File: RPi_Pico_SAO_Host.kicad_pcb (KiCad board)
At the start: 2 copper layers, 42 x 51.5 mm, 11 parts, among them J1 SAO Host Header, J2 SAO Host Header

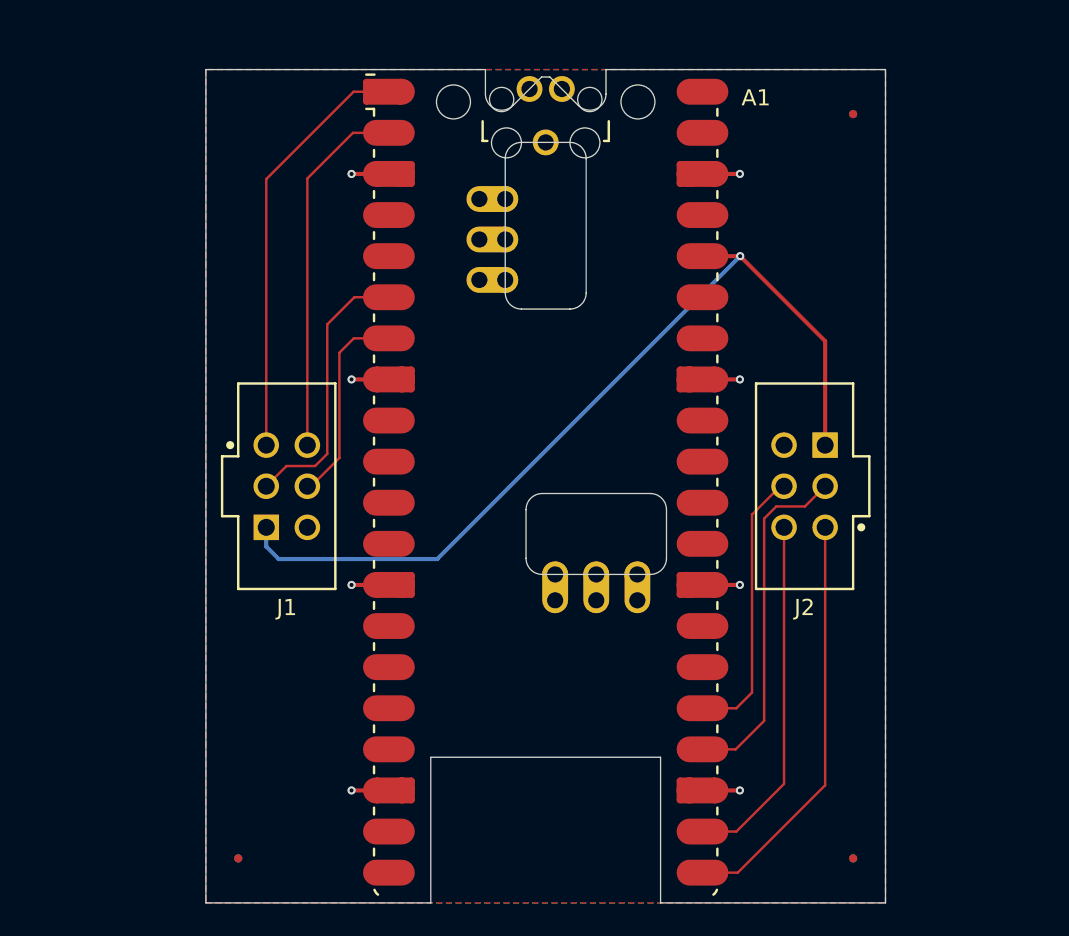
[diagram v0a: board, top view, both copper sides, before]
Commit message: Add v2 design changes
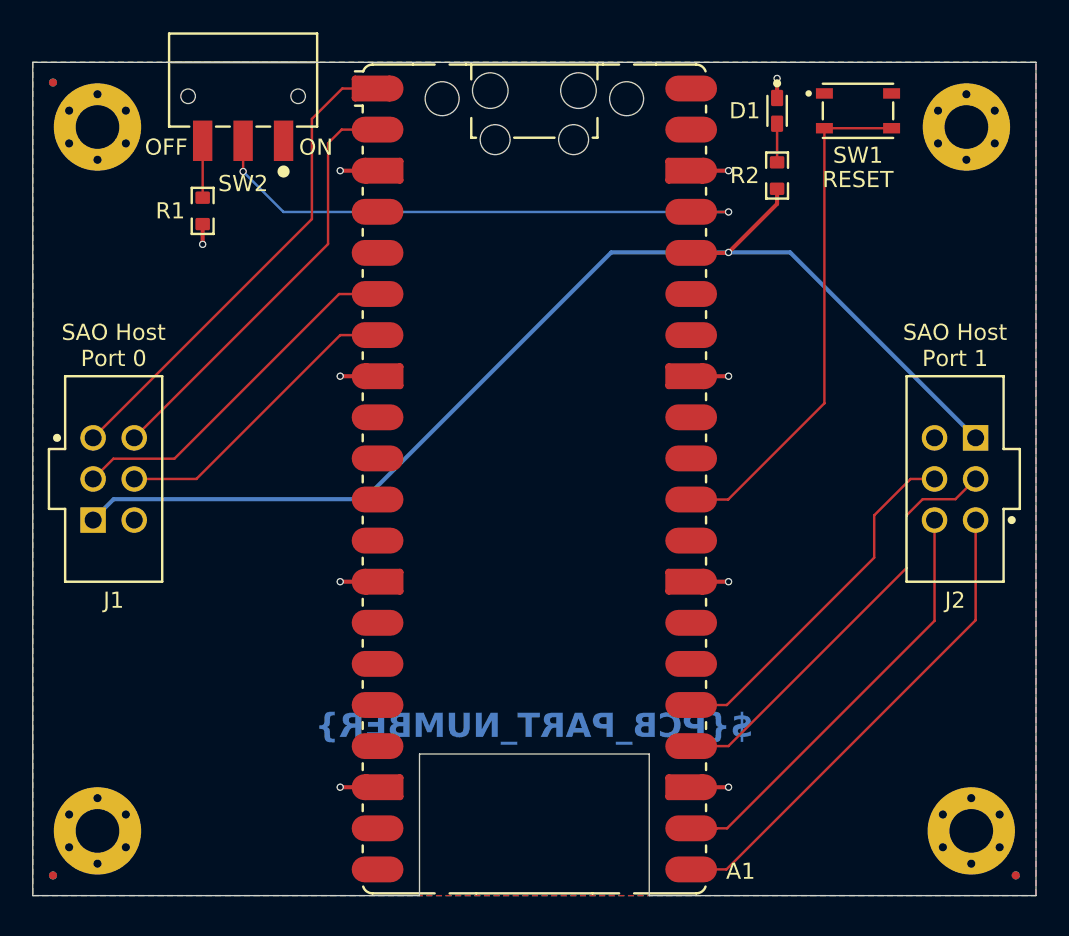
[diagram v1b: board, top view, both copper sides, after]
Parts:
- added D1: Green, CGND_LED:LEDSC_0603_0.8x1.6x0.8mm_L0.45x0.7mm_N, F.Cu at (154.0, 85.0)
- added H1: MTGNP_H2.1mm_M3.8mm_K4.2mm, CGND_Mounting_Hole:MTGNP_H2.1mm_M3.8mm_K4.2mm, F.Cu at (133.3, 84.2)
- added H2: MTGNP_H2.1mm_M3.8mm_K4.2mm, CGND_Mounting_Hole:MTGNP_H2.1mm_M3.8mm_K4.2mm, F.Cu at (144.7, 84.2)
- added H3: MTGP_5.4mm_H2.7mm_6V_H0.5mm, CGND_Mounting_Hole:MTGP_5.4mm_H2.7mm_6V_H0.5mm, F.Cu at (165.7, 86.0)
- added H4: MTGP_5.4mm_H2.7mm_6V_H0.5mm, CGND_Mounting_Hole:MTGP_5.4mm_H2.7mm_6V_H0.5mm, F.Cu at (166.0, 129.5)
- added H5: MTGP_5.4mm_H2.7mm_6V_H0.5mm, CGND_Mounting_Hole:MTGP_5.4mm_H2.7mm_6V_H0.5mm, F.Cu at (112.0, 129.5)
- added H6: MTGP_5.4mm_H2.7mm_6V_H0.5mm, CGND_Mounting_Hole:MTGP_5.4mm_H2.7mm_6V_H0.5mm, F.Cu at (112.0, 86.0)
- added LOGO3: Logo_WEEE_5.63x8mm_Silkscreen, CGND_Graphic:Logo_WEEE_5.63x8mm_Silkscreen, B.Cu at (150.0, 128.0)
- added LOGO4: Logo_ESD_8.74x7.93mm_Silkscreen, CGND_Graphic:Logo_ESD_8.74x7.93mm_Silkscreen, B.Cu at (158.0, 128.0)
- added LOGO5: Logo_KiCad_Designed_With_15.34x7.35mm_Silkscreen, CGND_Graphic:Logo_KiCad_Designed_With_15.34x7.35mm_Silkscreen, B.Cu at (123.0, 128.0)
- added OVERLAY1: SAO v2 Host Connector, CGND_Connector:Overlay_SAO_v2_Host, F.Cu at (113.0, 107.8)
- added OVERLAY2: SAO v2 Host Connector, CGND_Connector:Overlay_SAO_v2_Host, F.Cu at (165.0, 107.8)
- added R1: 100 Ω, CGND_Resistor:RESC_0603_1.6x0.8x0.55mm_L0.25mm_N, F.Cu at (118.5, 91.2)
- added R2: 560 Ω, CGND_Resistor:RESC_0603_1.6x0.8x0.55mm_L0.25mm_N, F.Cu at (154.0, 89.0)
- added SW1: PTS810SJM250SMTRLFS, CGND_Switch:CK_PTS810SJx250, F.Cu at (159.0, 85.0)
- added SW2: JS102011SAQN, CGND_Switch:CK_JS102011SAxN, F.Cu at (121.0, 83.1)
- added kibuzzard-68151D09: VAL**, kibuzzard-68151D09, B.Cu at (139.0, 95.0)
- A1: value RaspberryPi Pico W -> Raspberry Pi Pico; footprint RPi_Pico_SAO_Host:RASPBERRY_PI_PICO_W -> CGND_Module:Raspberry_Pi_Pico_Common_SMD
- FID1, FID2, FID3, FID4, FID5, FID6: value Fiducial -> FIDC_0.5mm_M1mm_K1mm_L; footprint RPi_Pico_SAO_Host:FIDC50M100K100L -> CGND_Fiducial:FIDC_0.5mm_M1mm_K1mm_L
- J1, J2: value SAO Host Header -> SFH11; footprint RPi_Pico_SAO_Host:SULLINS_SFH11-NBPC-D03-ST-BK_SAO_V2 -> CGND_Connector:Sullins_SFH11-xxxC-D03-ST-BK
- LOGO1: footprint RPi_Pico_SAO_Host:LOGO_OSHW_764X800_SILKSCREEN -> CGND_Graphic:Logo_OSHW_7.64x8mm_Silkscreen
- LOGO2: footprint RPi_Pico_SAO_Host:LOGO_CGND_700X700_SILKSCREEN -> CGND_Graphic:Logo_CGND_7x7mm_Silkscreen
- moved FID1 49.5 mm to (109.2, 83.2)
- moved FID4 49.5 mm to (109.2, 83.2)
- moved LOGO1 45.1 mm to (118.0, 119.0)
- moved LOGO2 18.5 mm to (139.0, 104.0)
- moved FID3 11.5 mm to (109.2, 132.2)
- moved FID6 11.5 mm to (109.2, 132.2)
- moved J1 10.7 mm to (113.0, 107.8)
- moved FID2 10.1 mm to (168.8, 132.2)
- moved FID5 10.1 mm to (168.8, 132.2)
- moved J2 9.31 mm to (165.0, 107.8)
- moved A1 0.73 mm to (139.0, 107.8)
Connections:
- net +3.3V renamed +3V3
- A1 pad 30: unconnected-(A1-RUN-Pad30) -> /~{RESET}
- A1 pad 37: unconnected-(A1-3V3_EN-Pad37) -> /PWR_EN
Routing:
- net /PWR_EN: track 0.00 -> 35.5 mm, vias 0 -> 2
- net /~{RESET}: track 0.00 -> 31.8 mm
- net +3V3: track 55.5 -> 73.7 mm
- net /SAO0_I2C_SCL: track 13.4 -> 18.7 mm
- net /SAO1_GPIO2: track 22.9 -> 28.2 mm
- net /SAO0_I2C_SDA: track 17.9 -> 22.3 mm
- net /SAO1_I2C_SCL: track 18.0 -> 22.4 mm
- net /SAO1_I2C_SDA: track 22.4 -> 26.3 mm
- net /SAO1_GPIO1: track 26.6 -> 30.1 mm
- net Net-(SW2-C): track 0.00 -> 3.52 mm
- net /SAO0_GPIO2: track 23.5 -> 26.6 mm
- net /SAO0_GPIO1: track 27.1 -> 30.1 mm
- net Net-(D1-Anode): track 0.00 -> 2.39 mm
- net GND: track 24.9 -> 26.5 mm, vias 8 -> 10
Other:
- board size 42 x 51.5 mm -> 62 x 51.5 mm
- board text added: "${ORGANIZATION} ${ORGANIZATION_URL}"
- board text added: "${PCB_PART_NUMBER}"
- board text added: "LABEL"
- board text added: "OFF"
- board text added: "ON"
- board text added: "PCB FABRICATOR MARKINGS"
- board text added: "PCB assembly notes 1. Assembly workmanship to meet or exceed the latest revision of IPC-A-610 Class 2. 2. Pb-free assembly process required. All materials, finishes, and processes used shall comply to the EU RoHS Directive 2002/95/EC. 3. Affix a combination serial number/bill of materials assembly part number/revision label in the {dblquote}LABEL{dblquote} area shown on the secondary side of the 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"
- board text added: "PCB fabrication notes 1. All dimensions are in millimeters (mm), unless otherwise specified. 2. All dimension tolerances are ±0.2 mm, unless otherwise specified. 3. Fabricate in accordance with IPC-6012 (latest revision), Class 2, per IPC-6011 using using the customer supplied master artwork ${PCB_PART_NUMBER} for the circuit pattern. No deviations from the master artwork are permitted without wr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"
- board text added: "Primary Side"
- board text added: "RESET"
- board text added: "SAO Host Port 0"
- board text added: "SAO Host Port 1"
- board text added: "Secondary Side"
- board text removed: "${COMPANY} ${COMPANY_URL}"
- board text removed: "Raspberry Pi Pico SAO Host v1"
